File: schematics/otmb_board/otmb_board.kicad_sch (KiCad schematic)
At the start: 3 parts, among them IC1 STM32U073CCT6, P1 USB_C_Plug_USB2.0, U1 TLV70212DBVT

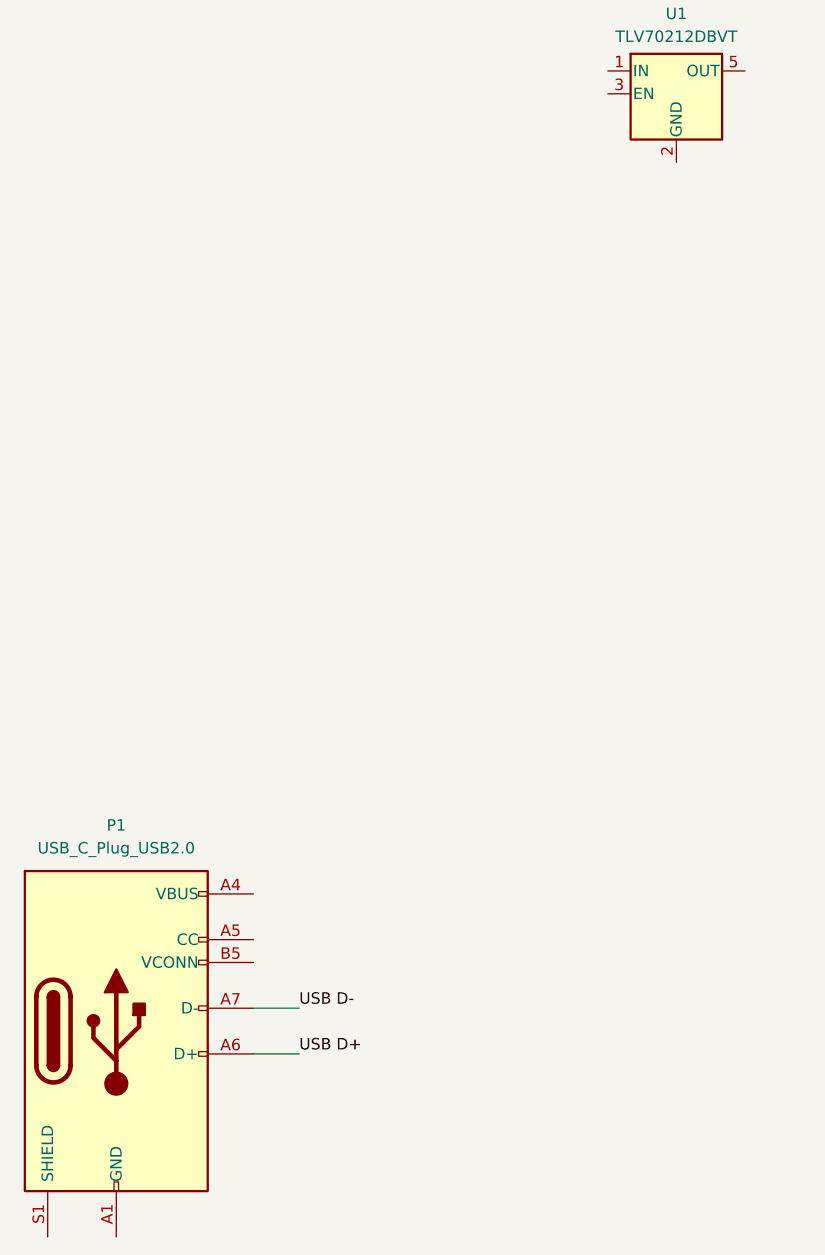
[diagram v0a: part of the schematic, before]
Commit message: Add USB C
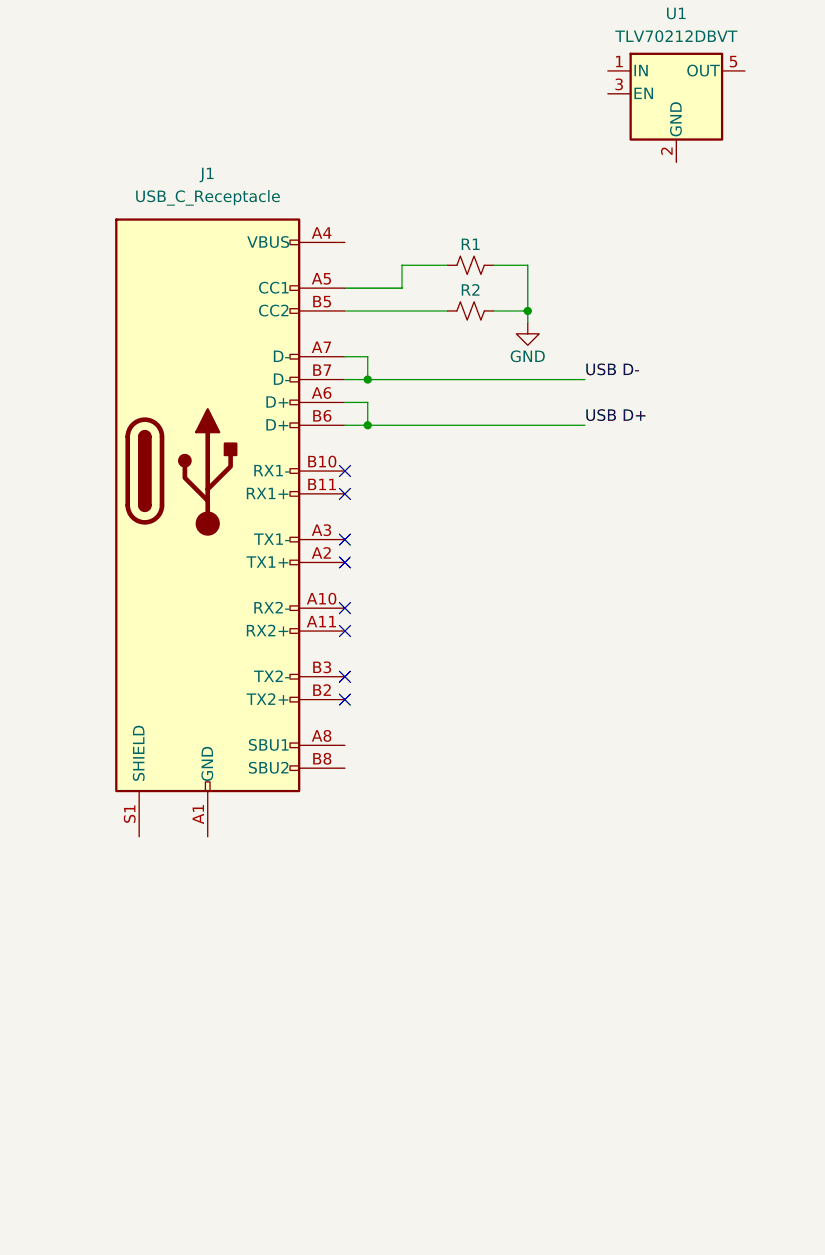
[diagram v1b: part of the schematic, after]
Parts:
- removed P1: USB_C_Plug_USB2.0, symbol Connector:USB_C_Plug_USB2.0
- added J1: USB_C_Receptacle, symbol Connector:USB_C_Receptacle
- added R1, R2: R_Small_US, symbol Device:R_Small_US
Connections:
- net USB D+: now also J1.A6 (D+), J1.B6 (D+)
- net USB D-: now also J1.A7 (D-), J1.B7 (D-)
- new net: J1.A5 (CC1), R1.1
- new net: J1.B5 (CC2), R2.1
- new net: J1.A1 (GND), J1.A12 (GND), J1.B1 (GND), J1.B12 (GND)
- new net: J1.A4 (VBUS), J1.A9 (VBUS), J1.B4 (VBUS), J1.B9 (VBUS)
- new net GND: R1.2, R2.2
- no-connect marks 0 -> 8

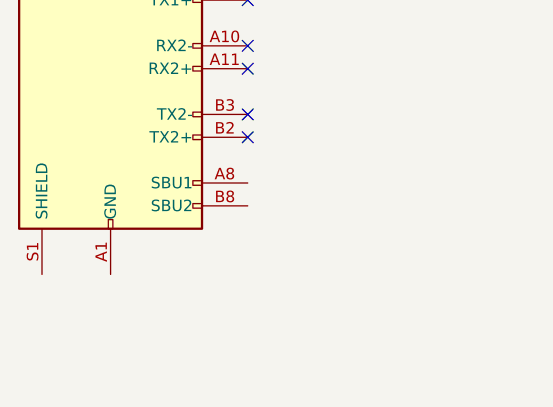
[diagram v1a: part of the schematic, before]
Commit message: Connect GND and Shield of USB C to GND
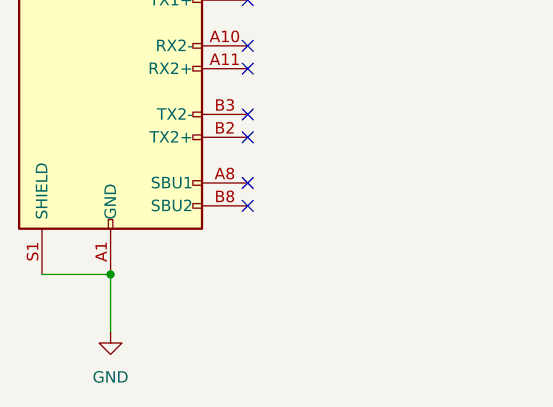
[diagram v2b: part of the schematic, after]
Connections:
- net GND: now also J1.A1 (GND), J1.A12 (GND), J1.B1 (GND), J1.B12 (GND), J1.S1 (SHIELD)
- no-connect marks 8 -> 10
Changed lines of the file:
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@@
 	(paper "A4")
+	(junction
+		(at 53.34 124.46)
+		(diameter 0)
+		(color 0 0 0 0)
+	)
 	(junction
 		(at 71.12 73.66)
@@
 	)
 	(no_connect
+		(at 68.58 114.3)
+	)
+	(no_connect
 		(at 68.58 83.82)
 	)
@@
 		(at 68.58 101.6)
 	)
+	(no_connect
+		(at 68.58 116.84)
+	)
 	(wire
 		(pts
@@
 	(wire
 		(pts
+			(xy 53.34 124.46) (xy 53.34 130.81)
+		)
+		(stroke
+			(width 0)
+			(type default)
+		)
+	)
+	(wire
+		(pts
 			(xy 74.93 63.5) (xy 74.93 60.96)
 		)
@@
 		(pts
 			(xy 180.34 93.98) (xy 186.69 93.98)
+		)
+		(stroke
+			(width 0)
+			(type default)
+		)
+	)
+	(wire
+		(pts
+			(xy 45.72 124.46) (xy 53.34 124.46)
 		)
 		(stroke
@@
 					(unit 1)
 				)
+			)
+		)
+	)
+	(symbol
+		(lib_id "power:GND")
+		(at 53.34 130.81 0)
+		(unit 1)
+		(exclude_from_sim no)
+		(in_bom yes)
+		(on_board yes)
+		(dnp no)
+		(fields_autoplaced yes)
+		(property "Reference" "#PWR02"
+			(at 53.34 137.16 0)
+			(effects
+				(font
+					(size 1.27 1.27)
+				)
+				(hide yes)
+			)
+		)
+		(property "Value" "GND"
+			(at 53.34 135.89 0)
+			(effects
+				(font
+					(size 1.27 1.27)
+				)
+			)
+		)
+		(property "Footprint" ""
+			(at 53.34 130.81 0)
+			(effects
+				(font
+					(size 1.27 1.27)
+				)
+				(hide yes)
+			)
+		)
+		(property "Datasheet" ""
+			(at 53.34 130.81 0)
+			(effects
+				(font
+					(size 1.27 1.27)
+				)
+				(hide yes)
+			)
+		)
+		(property "Description" "Power symbol creates a global label with name \"GND\" , ground"
+			(at 53.34 130.81 0)
+			(effects
+				(font
+					(size 1.27 1.27)
+				)
+				(hide yes)
+			)
+		)
+		(pin "1"
+		)
+		(instances
+			(project ""
+				(path "/f96461b7-7891-4a70-9cc7-4879d3904968"
+					(reference "#PWR02")
+					(unit 1)
+				)

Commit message: Connecting stuff to power
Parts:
- added D1, D2, D3, D4, D5: LED, symbol Device:LED
- added SW1: SW_SPST, symbol Switch:SW_SPST
- added U2: TPS2116DRL, Package_TO_SOT_SMD:SOT-583-8, symbol Power_Management:TPS2116DRL
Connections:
- net GND: now also IC1.35 (VSS_2), IC1.47 (VSS_3), IC1.8 (VSSA/VREF-), D1.1 (K), D2.1 (K), D3.1 (K), D4.1 (K), D5.1 (K), U2.1 (GND)
- net VDD: now reaches U1.5 (OUT)
- net VDD: now also IC1.1 (VBAT), IC1.36 (VDDUSB), IC1.48 (VDD_2), IC1.9 (VDDA/VREF+)
- net VCC: now reaches J1.A4 (VBUS), J1.A9 (VBUS), J1.B4 (VBUS), J1.B9 (VBUS)
- net VCC: now also U2.3 (VIN1)
- new net VBUS: U2.2 (VOUT), U2.7 (VOUT)
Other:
- moved on the sheet: U1

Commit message: More progress
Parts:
- added D6, D7: LED, symbol Device:LED
- added Q1, Q2, Q3, Q4, Q5, Q6: IRLZ44N, Package_TO_SOT_THT:TO-220-3_Vertical, symbol Transistor_FET:IRLZ44N
- added SW2: SW_SPST, symbol Switch:SW_SPST
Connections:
- net VBUS: now also U1.1 (IN)
- net VDD: now also SW2.2 (B)
- net at D4.2 (A): now also Q5.1 (G)
- net at D2.2 (A): now also Q3.1 (G)
- net at D1.2 (A): now also Q2.1 (G)
- net at D3.2 (A): now also Q4.1 (G)
- net at D5.2 (A): now also Q1.1 (G)
- net at IC1.13 (PA3): now also Q1.3 (S)
- net at IC1.14 (PA4): now also Q2.3 (S)
- net at IC1.15 (PA5): now also Q3.3 (S)
- net at IC1.16 (PA6): now also Q4.3 (S)
- net at IC1.17 (PA7): now also Q5.3 (S)
- net at IC1.18 (PB0): now also Q6.3 (S)
- net at IC1.44 (PF3-BOOT0): now also D6.1 (K)
- new net: D7.2 (A), Q6.1 (G)
- new net: D6.2 (A), SW2.1 (A)
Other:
- moved on the sheet: D5, SW1
